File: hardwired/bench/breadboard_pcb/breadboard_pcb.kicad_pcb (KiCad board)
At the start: 2 copper layers, 96.5 x 76.2 mm, 17 parts, among them J1 CV1, J2 CV2, J3 CV3, J4 CV4, J5 RJ45

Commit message: Simpler bb pcb
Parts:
- removed the J5 at (116.1, 49.5)
- added J+12V1: Conn_01x20_Pin, Connector_PinHeader_2.54mm:PinHeader_1x20_P2.54mm_Vertical, F.Cu at (88.9, 61.0)
- added J-12V1: Conn_01x20_Pin, Connector_PinHeader_2.54mm:PinHeader_1x20_P2.54mm_Vertical, F.Cu at (88.9, 100.3)
- added J10: Conn_01x05_Pin, Connector_PinHeader_2.54mm:PinHeader_1x05_P2.54mm_Vertical, F.Cu at (74.9, 54.6)
- added J5: Conn_01x05_Pin, Connector_PinHeader_2.54mm:PinHeader_1x05_P2.54mm_Vertical, F.Cu at (137.2, 85.1)
- added J5: Conn_01x05_Pin, Connector_PinHeader_2.54mm:PinHeader_1x05_P2.54mm_Vertical, F.Cu at (137.2, 66.0)
- added J6: Conn_01x26_Pin, Connector_PinHeader_2.54mm:PinHeader_1x26_P2.54mm_Vertical, F.Cu at (81.3, 80.0)
- added J7: Conn_01x05_Pin, Connector_PinHeader_2.54mm:PinHeader_1x05_P2.54mm_Vertical, F.Cu at (139.7, 55.9)
- added J8: Conn_01x05_Pin, Connector_PinHeader_2.54mm:PinHeader_1x05_P2.54mm_Vertical, F.Cu at (120.7, 55.9)
- added J9: Conn_01x05_Pin, Connector_PinHeader_2.54mm:PinHeader_1x05_P2.54mm_Vertical, F.Cu at (101.6, 55.9)
- C1, C2: value 1000u -> 100u; footprint Capacitor_THT:CP_Radial_D10.0mm_P5.00mm -> Capacitor_THT:CP_Radial_D5.0mm_P2.00mm
- D1, D2: footprint LED_THT:LED_D5.0mm_Clear -> LED_THT:LED_D3.0mm_Clear
- J1, J2, J3, J4: footprint Connector_Audio:Jack_3.5mm_QingPu_WQP-PJ398SM_Vertical_CircularHoles -> hardwired_footprints:ACJM-MV3-2S 3.5mm Audio Jack Mono Switched
- R3, R4, R5, R6: footprint Connector_PinHeader_2.54mm:PinHeader_1x03_P2.54mm_Vertical -> hardwired_footprints:BOURNS 2.54 335T POTENTIOMETER
- moved J3 18.5 mm to (107.9, 43.1), turned to 0 degrees
- moved R6 10.5 mm to (71.1, 25.4), turned to 0 degrees
- moved R5 9.64 mm to (94.0, 26.7), turned to 0 degrees
- moved R4 8.98 mm to (128.3, 26.7), turned to 0 degrees
- moved R3 8.89 mm to (146.1, 26.7), turned to 0 degrees
- moved J2 8.57 mm to (127.0, 43.2), turned to 0 degrees
- moved J4 8.57 mm to (81.3, 43.2), turned to 0 degrees
- moved J1 3.19 mm to (152.4, 42.6), turned to 0 degrees
- moved D2 1.27 mm to (74.9, 100.3)
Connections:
- net /GND renamed GND
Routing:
- net (no net): track 548.6 -> 10.2 mm, vias 270 -> 0
- net GND: track 510.7 -> 118.1 mm, vias 84 -> 0
- net -12V: track 267.9 -> 2.54 mm, vias 28 -> 0
- net +12V: track 234.4 -> 2.54 mm, vias 28 -> 0
- net /J1_T: track 39.7 -> 0.00 mm, vias 3 -> 0
- net /J4_T: track 39.5 -> 0.00 mm, vias 3 -> 0
- net /J2_T: track 33.7 -> 0.00 mm, vias 3 -> 0
- net /J3_T: track 33.4 -> 0.00 mm, vias 3 -> 0
- net /J3_TN: track 10.2 -> 0.00 mm
- net /LINE: track 0.00 -> 10.2 mm
- net /J4_TN: track 10.2 -> 0.00 mm
- net /J2_TN: track 10.2 -> 0.00 mm
- net /J1_TN: track 10.2 -> 0.00 mm
- net Net-(D2-A): track 5.08 -> 0.00 mm
- net Net-(D1-K): track 5.08 -> 0.00 mm

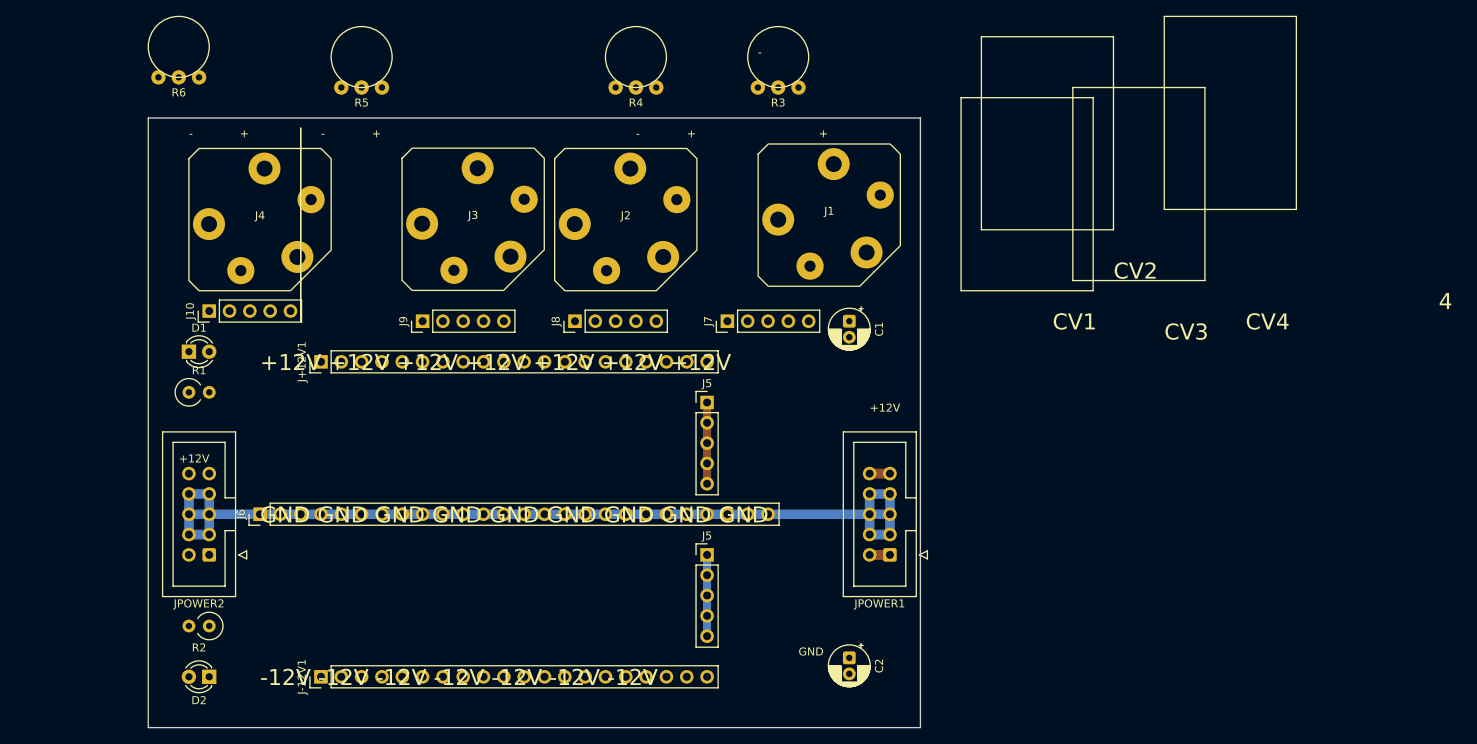
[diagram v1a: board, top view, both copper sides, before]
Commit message: Add improved breadboard PCB
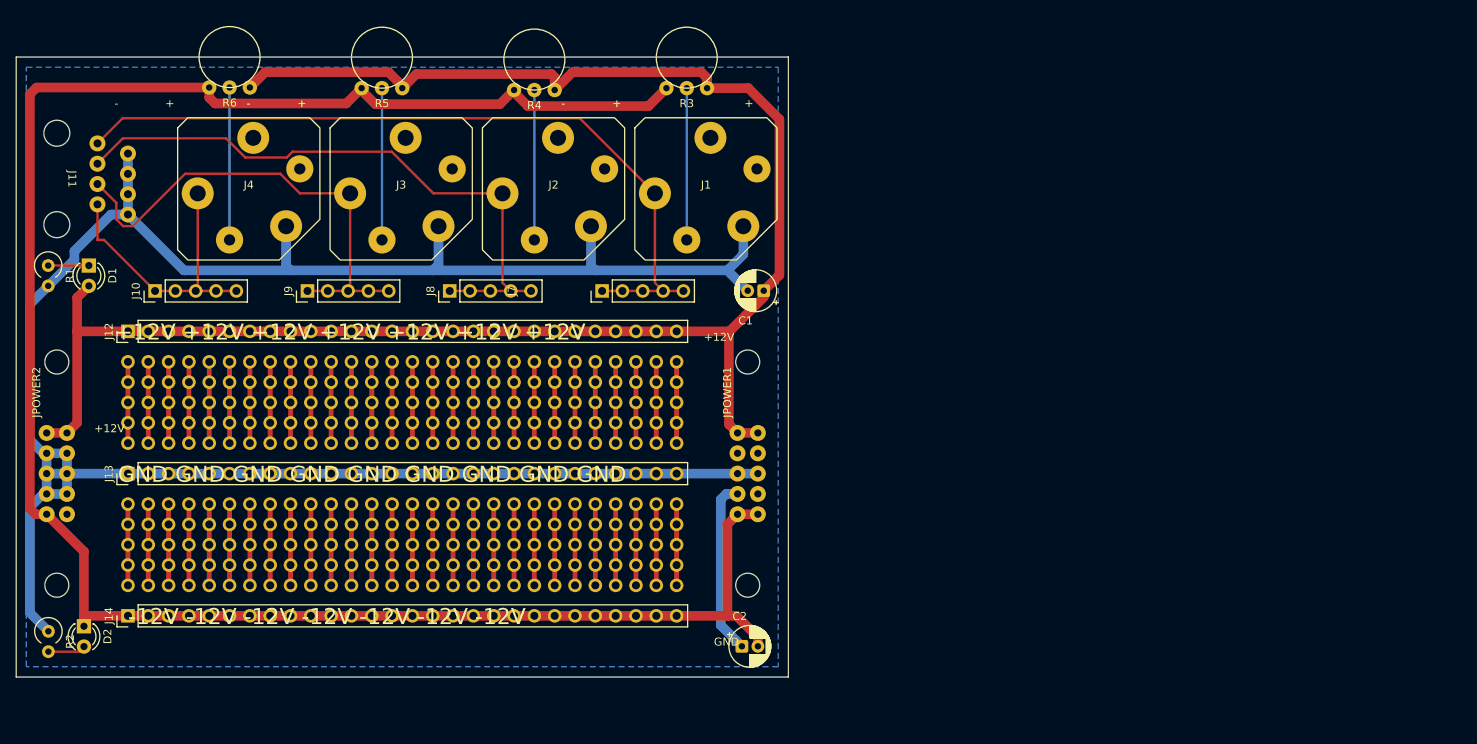
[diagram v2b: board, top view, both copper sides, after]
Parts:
- removed J+12V1, J-12V1: Conn_01x20_Pin, Connector_PinHeader_2.54mm:PinHeader_1x20_P2.54mm_Vertical
- removed J5 (x2): Conn_01x05_Pin, Connector_PinHeader_2.54mm:PinHeader_1x05_P2.54mm_Vertical
- removed J6: Conn_01x26_Pin, Connector_PinHeader_2.54mm:PinHeader_1x26_P2.54mm_Vertical
- added ?: , , F.Cu at (100.3, 71.1)
- added ?: , , F.Cu at (133.3, 83.8)
- added ?: , , F.Cu at (90.2, 63.5)
- added ?: , , F.Cu at (90.2, 61.0)
- added ?: , , F.Cu at (128.3, 61.0)
- added ?: , , F.Cu at (113.0, 78.7)
- added ?: , , F.Cu at (115.6, 78.7)
- added ?: , , F.Cu at (85.1, 78.7)
- added ?: , , F.Cu at (72.4, 81.3)
- added ?: , , F.Cu at (133.3, 88.9)
- added ?: , , F.Cu at (69.8, 71.1)
- added ?: , , F.Cu at (72.4, 78.7)
- added ?: , , F.Cu at (123.2, 71.1)
- added ?: , , F.Cu at (110.5, 61.0)
- added ?: , , F.Cu at (85.1, 88.9)
- added ?: , , F.Cu at (74.9, 83.8)
- added ?: , , F.Cu at (118.1, 66.0)
- added ?: , , F.Cu at (102.9, 88.9)
- added ?: , , F.Cu at (69.8, 83.8)
- added ?: , , F.Cu at (77.5, 68.6)
- added ?: , , F.Cu at (108.0, 83.8)
- added ?: , , F.Cu at (77.5, 88.9)
- added ?: , , F.Cu at (130.8, 86.4)
- added ?: , , F.Cu at (110.5, 78.7)
- added ?: , , F.Cu at (82.5, 83.8)
- added ?: , , F.Cu at (110.5, 86.4)
- added ?: , , F.Cu at (105.4, 63.5)
- added ?: , , F.Cu at (110.5, 88.9)
- added ?: , , F.Cu at (72.4, 61.0)
- added ?: , , F.Cu at (105.4, 68.6)
- added ?: , , F.Cu at (120.7, 61.0)
- added ?: , , F.Cu at (72.4, 88.9)
- added ?: , , F.Cu at (80.0, 71.1)
- added ?: , , F.Cu at (108.0, 78.7)
- added ?: , , F.Cu at (125.7, 66.0)
- added ?: , , F.Cu at (100.3, 86.4)
- added ?: , , F.Cu at (118.1, 78.7)
- added ?: , , F.Cu at (120.7, 81.3)
- added ?: , , F.Cu at (120.7, 66.0)
- added ?: , , F.Cu at (128.3, 63.5)
- added ?: , , F.Cu at (90.2, 88.9)
- added ?: , , F.Cu at (123.2, 63.5)
- added ?: , , F.Cu at (77.5, 63.5)
- added ?: , , F.Cu at (105.4, 61.0)
- added ?: , , F.Cu at (92.7, 88.9)
- added ?: , , F.Cu at (97.8, 61.0)
- added ?: , , F.Cu at (92.7, 66.0)
- added ?: , , F.Cu at (113.0, 71.1)
- added ?: , , F.Cu at (128.3, 88.9)
- added ?: , , F.Cu at (123.2, 66.0)
- added ?: , , F.Cu at (108.0, 66.0)
- added ?: , , F.Cu at (113.0, 88.9)
- added ?: , , F.Cu at (80.0, 86.4)
- added ?: , , F.Cu at (125.7, 88.9)
- added ?: , , F.Cu at (130.8, 66.0)
- added ?: , , F.Cu at (64.8, 78.7)
- added ?: , , F.Cu at (80.0, 83.8)
- added ?: , , F.Cu at (67.3, 83.8)
- added ?: , , F.Cu at (130.8, 71.1)
- added ?: , , F.Cu at (67.3, 61.0)
- added ?: , , F.Cu at (102.9, 83.8)
- added ?: , , F.Cu at (115.6, 83.8)
- added ?: , , F.Cu at (118.1, 81.3)
- added ?: , , F.Cu at (130.8, 88.9)
- added ?: , , F.Cu at (123.2, 81.3)
- added ?: , , F.Cu at (82.5, 61.0)
- added ?: , , F.Cu at (100.3, 81.3)
- added ?: , , F.Cu at (123.2, 86.4)
- added ?: , , F.Cu at (113.0, 61.0)
- added ?: , , F.Cu at (92.7, 61.0)
- added ?: , , F.Cu at (115.6, 71.1)
- added ?: , , F.Cu at (72.4, 63.5)
- added ?: , , F.Cu at (115.6, 61.0)
- added ?: , , F.Cu at (115.6, 63.5)
- added ?: , , F.Cu at (95.2, 68.6)
- added ?: , , F.Cu at (118.1, 63.5)
- added ?: , , F.Cu at (108.0, 86.4)
- added ?: , , F.Cu at (67.3, 88.9)
- added ?: , , F.Cu at (90.2, 66.0)
- added ?: , , F.Cu at (120.7, 63.5)
- added ?: , , F.Cu at (110.5, 71.1)
- added ?: , , F.Cu at (95.2, 86.4)
- added ?: , , F.Cu at (113.0, 63.5)
- added ?: , , F.Cu at (110.5, 68.6)
- added ?: , , F.Cu at (125.7, 83.8)
- added ?: , , F.Cu at (64.8, 66.0)
- added ?: , , F.Cu at (130.8, 83.8)
- added ?: , , F.Cu at (85.1, 63.5)
- added ?: , , F.Cu at (82.5, 68.6)
- added ?: , , F.Cu at (108.0, 81.3)
- added ?: , , F.Cu at (128.3, 68.6)
- added ?: , , F.Cu at (100.3, 63.5)
- added ?: , , F.Cu at (120.7, 78.7)
- added ?: , , F.Cu at (120.7, 83.8)
- added ?: , , F.Cu at (67.3, 81.3)
- added ?: , , F.Cu at (67.3, 71.1)
- added ?: , , F.Cu at (128.3, 78.7)
- added ?: , , F.Cu at (100.3, 88.9)
- added ?: , , F.Cu at (80.0, 88.9)
- added ?: , , F.Cu at (133.3, 81.3)
- added ?: , , F.Cu at (105.4, 81.3)
- added ?: , , F.Cu at (123.2, 68.6)
- added ?: , , F.Cu at (64.8, 68.6)
- added ?: , , F.Cu at (128.3, 81.3)
- added ?: , , F.Cu at (102.9, 86.4)
- added ?: , , F.Cu at (105.4, 71.1)
- added ?: , , F.Cu at (92.7, 63.5)
- added ?: , , F.Cu at (115.6, 81.3)
- added ?: , , F.Cu at (102.9, 81.3)
- added ?: , , F.Cu at (82.5, 88.9)
- added ?: , , F.Cu at (92.7, 78.7)
- added ?: , , F.Cu at (130.8, 68.6)
- added ?: , , F.Cu at (69.8, 88.9)
- added ?: , , F.Cu at (125.7, 81.3)
- added ?: , , F.Cu at (67.3, 68.6)
- added ?: , , F.Cu at (72.4, 68.6)
- added ?: , , F.Cu at (90.2, 83.8)
- added ?: , , F.Cu at (64.8, 61.0)
- added ?: , , F.Cu at (64.8, 71.1)
- added ?: , , F.Cu at (87.6, 88.9)
- added ?: , , F.Cu at (64.8, 63.5)
- added ?: , , F.Cu at (108.0, 68.6)
- added ?: , , F.Cu at (133.3, 63.5)
- added ?: , , F.Cu at (95.2, 71.1)
- added ?: , , F.Cu at (97.8, 68.6)
- added ?: , , F.Cu at (92.7, 68.6)
- added ?: , , F.Cu at (82.5, 86.4)
- added ?: , , F.Cu at (120.7, 88.9)
- added ?: , , F.Cu at (80.0, 68.6)
- added ?: , , F.Cu at (80.0, 66.0)
- added ?: , , F.Cu at (85.1, 81.3)
- added ?: , , F.Cu at (97.8, 83.8)
- added ?: , , F.Cu at (77.5, 71.1)
- added ?: , , F.Cu at (92.7, 86.4)
- added ?: , , F.Cu at (64.8, 86.4)
- added ?: , , F.Cu at (82.5, 66.0)
- added ?: , , F.Cu at (90.2, 68.6)
- added ?: , , F.Cu at (72.4, 83.8)
- added ?: , , F.Cu at (69.8, 63.5)
- added ?: , , F.Cu at (100.3, 68.6)
- added ?: , , F.Cu at (115.6, 68.6)
- added ?: , , F.Cu at (95.2, 61.0)
- added ?: , , F.Cu at (133.3, 71.1)
- added ?: , , F.Cu at (77.5, 83.8)
- added ?: , , F.Cu at (85.1, 83.8)
- added ?: , , F.Cu at (69.8, 66.0)
- added ?: , , F.Cu at (87.6, 78.7)
- added ?: , , F.Cu at (69.8, 86.4)
- added ?: , , F.Cu at (95.2, 81.3)
- added ?: , , F.Cu at (64.8, 81.3)
- added ?: , , F.Cu at (123.2, 61.0)
- added ?: , , F.Cu at (90.2, 78.7)
- added ?: , , F.Cu at (74.9, 68.6)
- added ?: , , F.Cu at (133.3, 61.0)
- added ?: , , F.Cu at (118.1, 88.9)
- added ?: , , F.Cu at (130.8, 81.3)
- added ?: , , F.Cu at (115.6, 66.0)
- added ?: , , F.Cu at (125.7, 78.7)
- added ?: , , F.Cu at (133.3, 86.4)
- added ?: , , F.Cu at (110.5, 66.0)
- added ?: , , F.Cu at (72.4, 71.1)
- added ?: , , F.Cu at (69.8, 81.3)
- added ?: , , F.Cu at (100.3, 78.7)
- added ?: , , F.Cu at (85.1, 71.1)
- added ?: , , F.Cu at (118.1, 68.6)
- added ?: , , F.Cu at (133.3, 78.7)
- added ?: , , F.Cu at (67.3, 78.7)
- added ?: , , F.Cu at (120.7, 68.6)
- added ?: , , F.Cu at (102.9, 68.6)
- added ?: , , F.Cu at (118.1, 61.0)
- added ?: , , F.Cu at (113.0, 66.0)
- added ?: , , F.Cu at (108.0, 88.9)
- added ?: , , F.Cu at (130.8, 78.7)
- added ?: , , F.Cu at (97.8, 66.0)
- added ?: , , F.Cu at (72.4, 66.0)
- added ?: , , F.Cu at (108.0, 61.0)
- added ?: , , F.Cu at (77.5, 86.4)
- added ?: , , F.Cu at (102.9, 78.7)
- added ?: , , F.Cu at (90.2, 81.3)
- added ?: , , F.Cu at (97.8, 88.9)
- added ?: , , F.Cu at (130.8, 61.0)
- added ?: , , F.Cu at (128.3, 71.1)
- added ?: , , F.Cu at (64.8, 83.8)
- added ?: , , F.Cu at (102.9, 61.0)
- added ?: , , F.Cu at (113.0, 83.8)
- added ?: , , F.Cu at (74.9, 63.5)
- added ?: , , F.Cu at (97.8, 63.5)
- added ?: , , F.Cu at (100.3, 66.0)
- added ?: , , F.Cu at (87.6, 66.0)
- added ?: , , F.Cu at (97.8, 81.3)
- added ?: , , F.Cu at (108.0, 63.5)
- added ?: , , F.Cu at (90.2, 86.4)
- added ?: , , F.Cu at (92.7, 83.8)
- added ?: , , F.Cu at (102.9, 66.0)
- added ?: , , F.Cu at (118.1, 71.1)
- added ?: , , F.Cu at (74.9, 86.4)
- added ?: , , F.Cu at (80.0, 63.5)
- added ?: , , F.Cu at (87.6, 83.8)
- added ?: , , F.Cu at (128.3, 86.4)
- added ?: , , F.Cu at (74.9, 78.7)
- added ?: , , F.Cu at (95.2, 78.7)
- added ?: , , F.Cu at (125.7, 61.0)
- added ?: , , F.Cu at (123.2, 88.9)
- added ?: , , F.Cu at (80.0, 81.3)
- added ?: , , F.Cu at (87.6, 61.0)
- added ?: , , F.Cu at (128.3, 66.0)
- added ?: , , F.Cu at (105.4, 83.8)
- added ?: , , F.Cu at (110.5, 63.5)
- added ?: , , F.Cu at (123.2, 83.8)
- added ?: , , F.Cu at (72.4, 86.4)
- added ?: , , F.Cu at (85.1, 61.0)
- added ?: , , F.Cu at (95.2, 63.5)
- added ?: , , F.Cu at (125.7, 68.6)
- added ?: , , F.Cu at (92.7, 81.3)
- added ?: , , F.Cu at (82.5, 63.5)
- added ?: , , F.Cu at (110.5, 81.3)
- added ?: , , F.Cu at (77.5, 61.0)
- added ?: , , F.Cu at (105.4, 88.9)
- added ?: , , F.Cu at (85.1, 68.6)
- added ?: , , F.Cu at (133.3, 66.0)
- added ?: , , F.Cu at (92.7, 71.1)
- added ?: , , F.Cu at (74.9, 66.0)
- added ?: , , F.Cu at (97.8, 78.7)
- added ?: , , F.Cu at (74.9, 71.1)
- added ?: , , F.Cu at (67.3, 66.0)
- added ?: , , F.Cu at (87.6, 68.6)
- added ?: , , F.Cu at (77.5, 81.3)
- added ?: , , F.Cu at (85.1, 66.0)
- added ?: , , F.Cu at (95.2, 88.9)
- added ?: , , F.Cu at (118.1, 83.8)
- added ?: , , F.Cu at (69.8, 61.0)
- added ?: , , F.Cu at (80.0, 78.7)
- added ?: , , F.Cu at (90.2, 71.1)
- added ?: , , F.Cu at (97.8, 71.1)
- added ?: , , F.Cu at (105.4, 66.0)
- added ?: , , F.Cu at (85.1, 86.4)
- added ?: , , F.Cu at (130.8, 63.5)
- added ?: , , F.Cu at (67.3, 86.4)
- added ?: , , F.Cu at (77.5, 66.0)
- added ?: , , F.Cu at (87.6, 81.3)
- added ?: , , F.Cu at (118.1, 86.4)
- added ?: , , F.Cu at (123.2, 78.7)
- added ?: , , F.Cu at (82.5, 71.1)
- added ?: , , F.Cu at (102.9, 71.1)
- added ?: , , F.Cu at (69.8, 68.6)
- added ?: , , F.Cu at (125.7, 86.4)
- added ?: , , F.Cu at (95.2, 83.8)
- added ?: , , F.Cu at (120.7, 71.1)
- added ?: , , F.Cu at (87.6, 71.1)
- added ?: , , F.Cu at (133.3, 68.6)
- added ?: , , F.Cu at (113.0, 68.6)
- added ?: , , F.Cu at (77.5, 78.7)
- added ?: , , F.Cu at (105.4, 86.4)
- added ?: , , F.Cu at (74.9, 88.9)
- added ?: , , F.Cu at (64.8, 88.9)
- added ?: , , F.Cu at (97.8, 86.4)
- added ?: , , F.Cu at (113.0, 86.4)
- added ?: , , F.Cu at (67.3, 63.5)
- added ?: , , F.Cu at (105.4, 78.7)
- added ?: , , F.Cu at (128.3, 83.8)
- added ?: , , F.Cu at (74.9, 81.3)
- added ?: , , F.Cu at (74.9, 61.0)
- added ?: , , F.Cu at (125.7, 63.5)
- added ?: , , F.Cu at (115.6, 86.4)
- added ?: , , F.Cu at (100.3, 83.8)
- added ?: , , F.Cu at (113.0, 81.3)
- added ?: , , F.Cu at (82.5, 81.3)
- added ?: , , F.Cu at (125.7, 71.1)
- added ?: , , F.Cu at (110.5, 83.8)
- added ?: , , F.Cu at (87.6, 63.5)
- added ?: , , F.Cu at (108.0, 71.1)
- added ?: , , F.Cu at (82.5, 78.7)
- added ?: , , F.Cu at (69.8, 78.7)
- added ?: , , F.Cu at (80.0, 61.0)
- added ?: , , F.Cu at (95.2, 66.0)
- added ?: , , F.Cu at (102.9, 63.5)
- added ?: , , F.Cu at (87.6, 86.4)
- added ?: , , F.Cu at (100.3, 61.0)
- added ?: , , F.Cu at (120.7, 86.4)
- added ?: , , F.Cu at (115.6, 88.9)
- added J11: RJ45, hardwired_footprints:Keystone RJ45 949, F.Cu at (55.9, 38.1)
- added J12: Conn_01x28_Pin, Connector_PinHeader_2.54mm:PinHeader_1x28_P2.54mm_Vertical, F.Cu at (64.8, 57.1)
- added J13: Conn_01x28_Pin, Connector_PinHeader_2.54mm:PinHeader_1x28_P2.54mm_Vertical, F.Cu at (64.8, 74.9)
- added J14: Conn_01x28_Pin, Connector_PinHeader_2.54mm:PinHeader_1x28_P2.54mm_Vertical, F.Cu at (64.8, 92.7)
- JPOWER1, JPOWER2: footprint Connector_IDC:IDC-Header_2x05_P2.54mm_Vertical -> hardwired_footprints:Amphenol 71918-110LF 2.54 2x05 IDC
- moved R1 23.7 mm to (54.8, 48.9), turned to -90 degrees
- moved JPOWER2 21.6 mm to (55.9, 74.9), turned to 90 degrees
- moved JPOWER1 20.5 mm to (142.2, 74.9), turned to 90 degrees
- moved R2 20.1 mm to (54.8, 94.6), turned to -90 degrees
- moved D2 16.9 mm to (59.3, 94.0), turned to -90 degrees
- moved D1 16.5 mm to (59.9, 48.9), turned to -90 degrees
- moved J8 16.1 mm to (105.0, 52.1)
- moved J7 16.1 mm to (124.0, 52.1)
- moved J1 15.8 mm to (137.0, 39.3)
- moved J9 14.9 mm to (87.2, 52.1)
- moved C2 13.5 mm to (141.5, 96.5), turned to 0 degrees
- moved R4 12.7 mm to (115.6, 27.0)
- moved R3 11.4 mm to (134.6, 26.8)
- moved C1 11.4 mm to (144.2, 52.1), turned to 180 degrees
- moved J2 9.81 mm to (118.0, 39.3)
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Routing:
- net (no net): track 10.2 -> 569.0 mm
- net -12V: track 2.54 -> 258.3 mm
- net +12V: track 2.54 -> 223.0 mm
- net GND: track 118.1 -> 295.2 mm
- net /J1_T: track 0.00 -> 97.7 mm
- net /J2_T: track 0.00 -> 78.2 mm
- net /J3_T: track 0.00 -> 61.1 mm
- net /J4_T: track 0.00 -> 36.8 mm
- net /J4_TN: track 0.00 -> 19.0 mm
- net /J3_TN: track 0.00 -> 19.0 mm
- net /J1_TN: track 0.00 -> 19.0 mm
- net /J2_TN: track 0.00 -> 18.7 mm
- net /LINE: track 10.2 -> 0.00 mm
- net Net-(D1-K): track 0.00 -> 5.08 mm
- net Net-(D2-A): track 0.00 -> 4.71 mm
- added copper zone on B.Cu, net GND
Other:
- board size 96.5 x 76.2 mm -> 96.5 x 77.5 mm
- board text removed: "4"
- board text removed: "CV1"
- board text removed: "CV2"
- board text removed: "CV3"
- board text removed: "CV4"
